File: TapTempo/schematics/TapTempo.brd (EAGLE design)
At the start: 60.6 x 50.3 mm, 46 parts, among them IC1 MEGA168, IC2 MCP4921, IC3 TL072D, IC4 LM4041A12DBZ, Q301 BC846, Q701 BC846, Y1 16Mhz

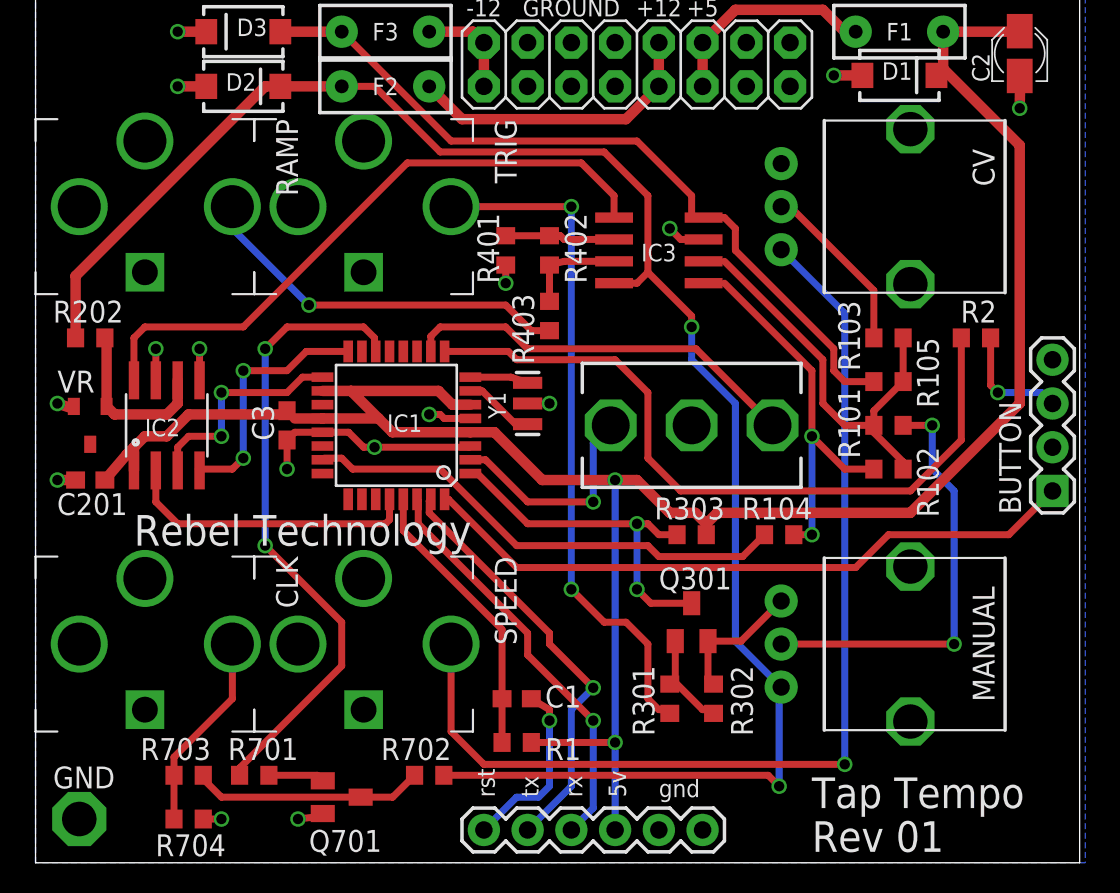
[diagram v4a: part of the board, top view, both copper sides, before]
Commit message: verified with Seeed dru - bigger pads
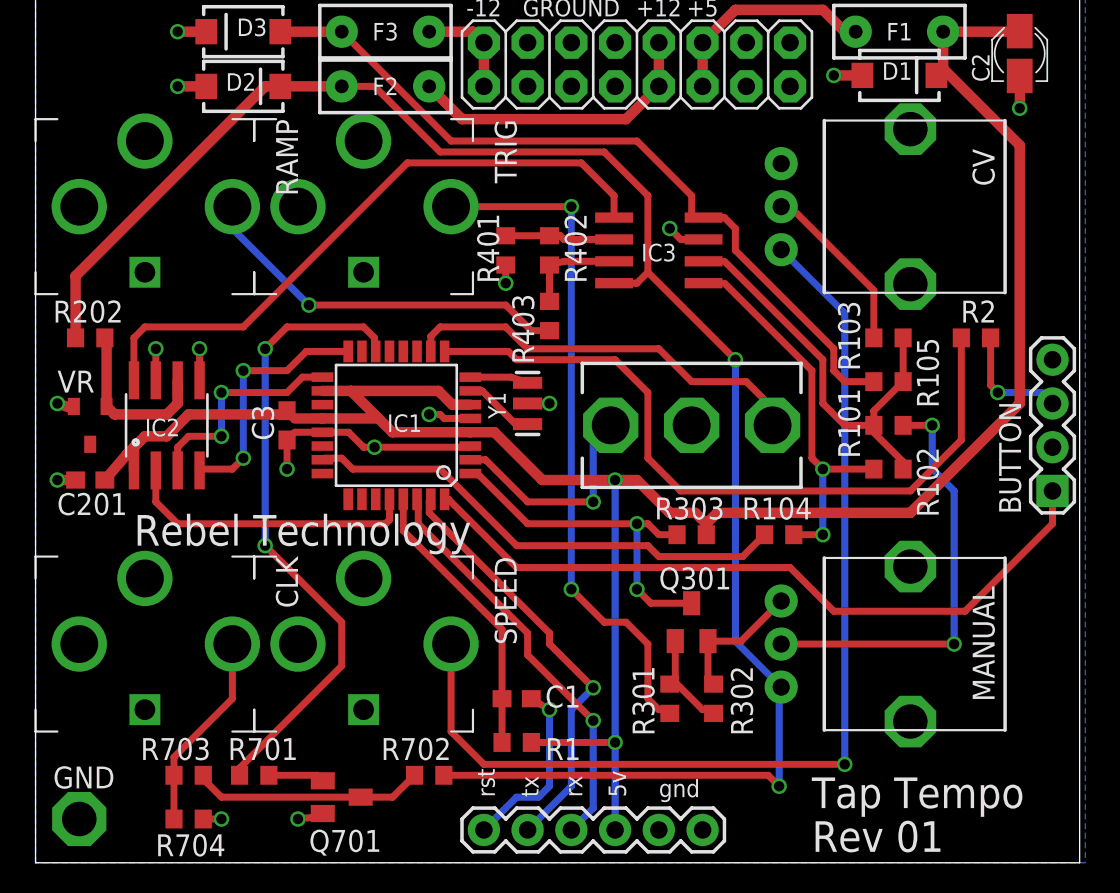
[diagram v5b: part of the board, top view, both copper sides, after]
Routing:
- net SW1: track 38.8 -> 42.0 mm
- net MODESW: track 23.3 -> 23.9 mm
- net N$4: track 23.4 -> 22.8 mm
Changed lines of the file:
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@@
 </class>
 </classes>
-<designrules name="default">
-<description language="de">
-&lt;b&gt;Rebel Rules&lt;/b&gt;
+<designrules name="Fusion_eagle_rule_v1.1">
+<description language="de">&lt;b&gt;EAGLE Design Rules&lt;/b&gt;
 &lt;p&gt;
-</description>
-<description language="en">
-&lt;b&gt;Rebel Rules&lt;/b&gt;
+Die Standard-Design-Rules sind so gewählt, dass sie für
+die meisten Anwendungen passen. Sollte ihre Platine
+besondere Anforderungen haben, treffen Sie die erforderlichen
+Einstellungen hier und speichern die Design Rules unter
+einem neuen Namen ab.</description>
+<description language="en">&lt;b&gt;EAGLE Design Rules&lt;/b&gt;
 &lt;p&gt;
-</description>
-<description language="zh">
-&lt;b&gt;Rebel Rules&lt;/b&gt;
-&lt;p&gt;
+The default Design Rules have been set to cover
+a wide range of applications. Your particular design
+may have different requirements, so please make the
+necessary adjustments and save your customized
+design rules under a new name.</description>
+<description language="zh">&lt;b&gt;Seeed Studio EAGLE Design Rules&lt;/b&gt;
 </description>
 <param name="layerSetup" value="(1*16)"/>
 <param name="mtCopper" value="0.035mm 0.035mm 0.035mm 0.035mm 0.035mm 0.035mm 0.035mm 0.035mm 0.035mm 0.035mm 0.035mm 0.035mm 0.035mm 0.035mm 0.035mm 0.035mm"/>
 <param name="mtIsolate" value="1.5mm 0.15mm 0.2mm 0.15mm 0.2mm 0.15mm 0.2mm 0.15mm 0.2mm 0.15mm 0.2mm 0.15mm 0.2mm 0.15mm 0.2mm"/>
-<param name="mdWireWire" value="8mil"/>
-<param name="mdWirePad" value="8mil"/>
-<param name="mdWireVia" value="8mil"/>
-<param name="mdPadPad" value="8mil"/>
-<param name="mdPadVia" value="8mil"/>
-<param name="mdViaVia" value="8mil"/>
+<param name="mdWireWire" value="6mil"/>
+<param name="mdWirePad" value="6mil"/>
+<param name="mdWireVia" value="6mil"/>
+<param name="mdPadPad" value="6mil"/>
+<param name="mdPadVia" value="6mil"/>
+<param name="mdViaVia" value="6mil"/>
 <param name="mdSmdPad" value="0mil"/>
 <param name="mdSmdVia" value="0mil"/>
@@
 <param name="rvMicroViaOuter" value="0.25"/>
 <param name="rvMicroViaInner" value="0.25"/>
-<param name="rlMinPadTop" value="12mil"/>
-<param name="rlMaxPadTop" value="16mil"/>
-<param name="rlMinPadInner" value="12mil"/>
-<param name="rlMaxPadInner" value="16mil"/>
-<param name="rlMinPadBottom" value="12mil"/>
-<param name="rlMaxPadBottom" value="16mil"/>
+<param name="rlMinPadTop" value="10mil"/>
+<param name="rlMaxPadTop" value="20mil"/>
+<param name="rlMinPadInner" value="10mil"/>
+<param name="rlMaxPadInner" value="20mil"/>
+<param name="rlMinPadBottom" value="10mil"/>
+<param name="rlMaxPadBottom" value="20mil"/>
 <param name="rlMinViaOuter" value="6mil"/>
 <param name="rlMaxViaOuter" value="20mil"/>
@@
 <wire x1="17.78" y1="45.085" x2="19.685" y2="45.085" width="0.4064" layer="1"/>
 <wire x1="19.685" y1="45.085" x2="23.495" y2="41.275" width="0.4064" layer="1"/>
-<wire x1="40.64" y1="26.67" x2="40.64" y2="12.86" width="0.4064" layer="16"/>
+<wire x1="40.64" y1="29.21" x2="40.64" y2="12.86" width="0.4064" layer="16"/>
 <wire x1="40.64" y1="12.86" x2="43.3" y2="10.2" width="0.4064" layer="16"/>
 <contactref element="R702" pad="1"/>
@@
 <wire x1="43.18" y1="4.445" x2="43.18" y2="10.08" width="0.4064" layer="16"/>
 <wire x1="43.18" y1="10.08" x2="43.3" y2="10.2" width="0.4064" layer="16"/>
-<wire x1="38.1" y1="29.21" x2="40.64" y2="26.67" width="0.4064" layer="16"/>
 <wire x1="23.495" y1="41.275" x2="33.02" y2="41.275" width="0.4064" layer="1"/>
 <wire x1="33.02" y1="41.275" x2="35.56" y2="38.735" width="0.4064" layer="1"/>
@@
 <wire x1="42.545" y1="5.08" x2="43.18" y2="4.445" width="0.4064" layer="1"/>
 <wire x1="35.56" y1="38.735" x2="35.56" y2="34.29" width="0.4064" layer="1"/>
-<via x="38.1" y="31.115" extent="1-16" drill="0.6" shape="square"/>
-<wire x1="38.1" y1="31.115" x2="38.1" y2="29.21" width="0.4064" layer="16"/>
+<via x="40.64" y="29.21" extent="1-16" drill="0.6" shape="square"/>
 <wire x1="33.595" y1="33.655" x2="34.925" y2="33.655" width="0.4064" layer="1"/>
 <wire x1="34.925" y1="33.655" x2="35.56" y2="34.29" width="0.4064" layer="1"/>
-<wire x1="35.56" y1="34.29" x2="38.1" y2="31.75" width="0.4064" layer="1"/>
-<wire x1="38.1" y1="31.75" x2="38.1" y2="31.115" width="0.4064" layer="1"/>
+<wire x1="35.56" y1="34.29" x2="40.64" y2="29.21" width="0.4064" layer="1"/>
 </signal>
 <signal name="N$2">
@@
 <contactref element="R104" pad="1"/>
 <contactref element="R102" pad="2"/>
-<wire x1="48.68" y1="22.86" x2="46.99" y2="22.86" width="0.4064" layer="1"/>
-<wire x1="46.99" y1="22.86" x2="45.085" y2="24.765" width="0.4064" layer="1"/>
+<wire x1="48.68" y1="22.86" x2="45.72" y2="22.86" width="0.4064" layer="1"/>
 <wire x1="38.795" y1="33.655" x2="40.005" y2="33.655" width="0.3048" layer="1"/>
-<wire x1="45.085" y1="24.765" x2="45.085" y2="28.575" width="0.4064" layer="1"/>
 <wire x1="45.085" y1="28.575" x2="40.005" y2="33.655" width="0.4064" layer="1"/>
-<via x="45.085" y="19.05" extent="1-16" drill="0.6" shape="square"/>
-<wire x1="45.085" y1="19.05" x2="45.085" y2="24.765" width="0.4064" layer="16"/>
-<via x="45.085" y="24.765" extent="1-16" drill="0.6" shape="square"/>
-<wire x1="44.03" y1="19.05" x2="45.085" y2="19.05" width="0.4064" layer="1"/>
+<via x="45.72" y="19.05" extent="1-16" drill="0.6" shape="square"/>
+<wire x1="45.72" y1="19.05" x2="45.72" y2="22.86" width="0.4064" layer="16"/>
+<via x="45.72" y="22.86" extent="1-16" drill="0.6" shape="square"/>
+<wire x1="44.03" y1="19.05" x2="45.72" y2="19.05" width="0.4064" layer="1"/>
+<wire x1="45.085" y1="28.575" x2="45.085" y2="23.495" width="0.4064" layer="1"/>
+<wire x1="45.085" y1="23.495" x2="45.72" y2="22.86" width="0.4064" layer="1"/>
 </signal>
 <signal name="-12V">
@@
 <contactref element="JP1" pad="6"/>
 <contactref element="C1" pad="1"/>
-<via x="29.845" y="8.255" extent="1-16" drill="0.6" shape="square"/>
-<wire x1="29.845" y1="8.255" x2="29.845" y2="4.445" width="0.4064" layer="16"/>
+<via x="29.845" y="8.89" extent="1-16" drill="0.6" shape="square"/>
+<wire x1="29.845" y1="8.89" x2="29.845" y2="4.445" width="0.4064" layer="16"/>
 <wire x1="29.845" y1="4.445" x2="29.21" y2="3.81" width="0.4064" layer="16"/>
 <wire x1="29.21" y1="3.81" x2="27.94" y2="3.81" width="0.4064" layer="16"/>
 <wire x1="27.94" y1="3.81" x2="26.035" y2="1.905" width="0.4064" layer="16"/>
-<wire x1="29.845" y1="8.255" x2="29.845" y2="8.89" width="0.4064" layer="1"/>
 <wire x1="29.845" y1="8.89" x2="28.79" y2="9.525" width="0.4064" layer="1"/>
 </signal>
@@
 <contactref element="IC1" pad="10"/>
 <wire x1="22.955" y1="29.6926" x2="22.955" y2="30.575" width="0.4064" layer="1"/>
-<wire x1="28.575" y1="29.845" x2="38.354" y2="29.845" width="0.4064" layer="1"/>
-<wire x1="38.354" y1="29.845" x2="42.799" y2="25.4" width="0.4064" layer="1"/>
+<wire x1="28.575" y1="29.845" x2="36.195" y2="29.845" width="0.4064" layer="1"/>
 <wire x1="22.955" y1="30.575" x2="23.495" y2="31.115" width="0.4064" layer="1"/>
 <wire x1="23.495" y1="31.115" x2="27.305" y2="31.115" width="0.4064" layer="1"/>
 <wire x1="27.305" y1="31.115" x2="28.575" y2="29.845" width="0.4064" layer="1"/>
+<wire x1="36.195" y1="29.845" x2="38.1" y2="27.94" width="0.4064" layer="1"/>
+<wire x1="42.799" y1="25.4" x2="42.799" y2="26.416" width="0.4064" layer="1"/>
+<wire x1="42.799" y1="26.416" x2="41.275" y2="27.94" width="0.4064" layer="1"/>
+<wire x1="41.275" y1="27.94" x2="38.1" y2="27.94" width="0.4064" layer="1"/>
 </signal>
 <signal name="N$28">
@@
 <wire x1="23.755" y1="21.1074" x2="23.9776" y2="21.1074" width="0.4064" layer="1"/>
 <wire x1="23.9776" y1="21.1074" x2="27.94" y2="17.145" width="0.4064" layer="1"/>
-<wire x1="27.94" y1="17.145" x2="47.625" y2="17.145" width="0.4064" layer="1"/>
-<wire x1="47.625" y1="17.145" x2="49.53" y2="19.05" width="0.4064" layer="1"/>
-<wire x1="49.53" y1="19.05" x2="56.515" y2="19.05" width="0.4064" layer="1"/>
-<wire x1="56.515" y1="19.05" x2="59.055" y2="21.59" width="0.4064" layer="1"/>
+<wire x1="27.94" y1="17.145" x2="43.815" y2="17.145" width="0.4064" layer="1"/>
+<wire x1="43.815" y1="17.145" x2="46.355" y2="14.605" width="0.4064" layer="1"/>
+<wire x1="46.355" y1="14.605" x2="53.975" y2="14.605" width="0.4064" layer="1"/>
+<wire x1="53.975" y1="14.605" x2="59.055" y2="19.685" width="0.4064" layer="1"/>
+<wire x1="59.055" y1="19.685" x2="59.055" y2="21.59" width="0.4064" layer="1"/>
 </signal>
 <signal name="SDI">
